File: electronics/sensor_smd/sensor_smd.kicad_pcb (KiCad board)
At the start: 2 copper layers, 40 x 20 mm, 7 parts, among them J1 HEADER MALE RA, U1 HX6286

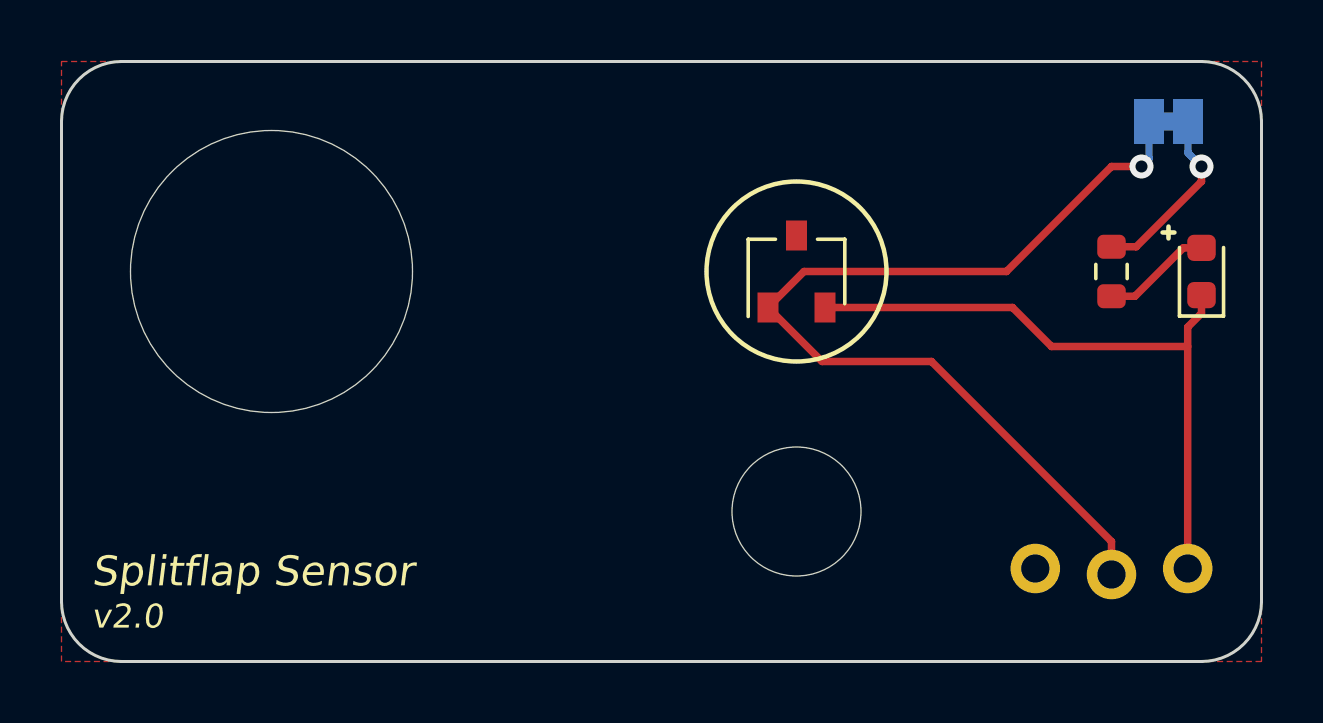
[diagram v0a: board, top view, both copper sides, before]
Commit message: Move hall effect sensor further in to allow for smaller spools
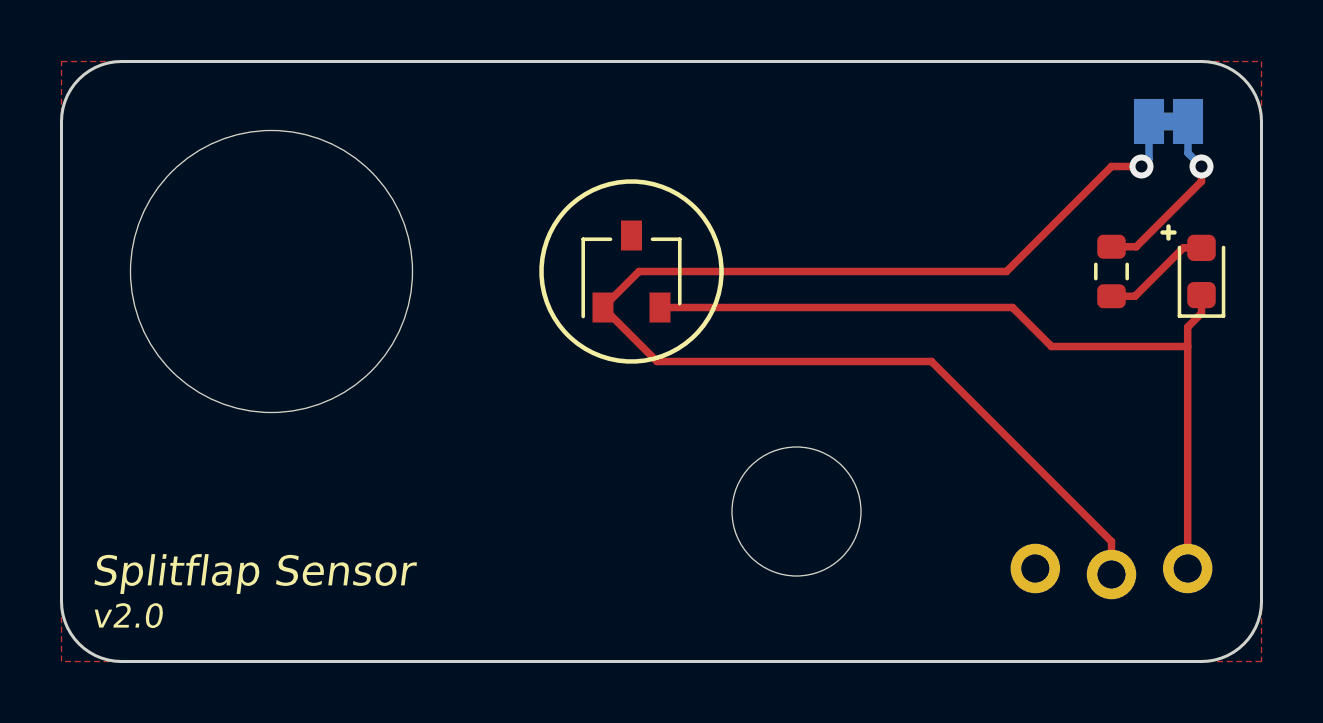
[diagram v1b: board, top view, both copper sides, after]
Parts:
- moved U1 5.50 mm to (112.0, 100.0)
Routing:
- net VDD: track 31.8 -> 42.8 mm
- net /SIGNAL: track 21.9 -> 27.4 mm
